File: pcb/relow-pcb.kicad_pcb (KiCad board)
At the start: 2 copper layers, 76.2 x 44.5 mm, 75 parts, among them IC1 AD8495, IC2 ATMEGA328P_TQFP, IC3 FT230X_SOP, J1 MICROUSB, J2 TOASTER, K1 S212S01, M3 VAL**, P1 AVR_ISP, Q1 MMBT4401, Q2 MMBT4401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

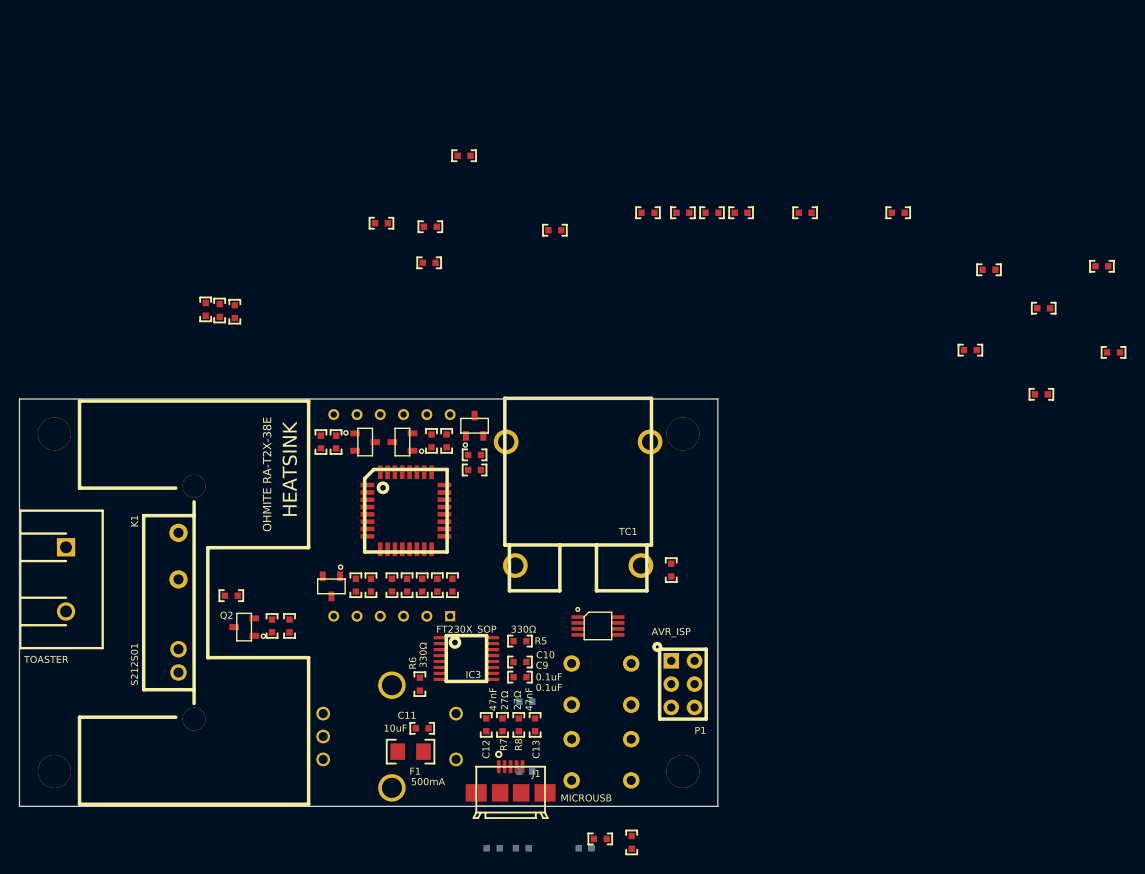
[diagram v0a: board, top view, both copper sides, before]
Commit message: components placed. starting traces
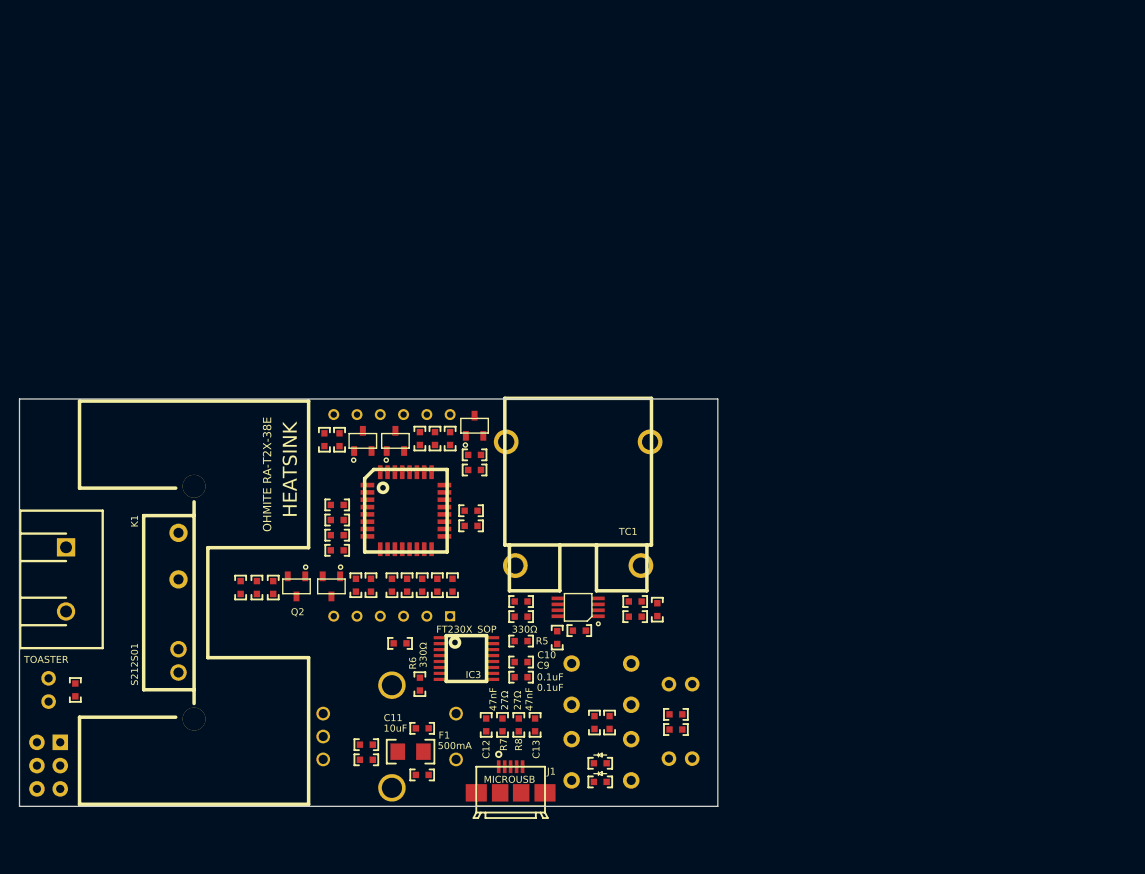
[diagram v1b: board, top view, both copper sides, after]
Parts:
- removed M3 (x4): VAL**, M3
- LED1, LED2: moved to F.Cu
- LED3, LED4, LED5: footprint 0603(1608m)_led -> LED-5mm
- P1: moved to B.Cu
- R18: value 1kΩ -> 330Ω
- moved R11 85.4 mm to (137.5, 157.1)
- moved R1 84.1 mm to (141.2, 146.1)
- moved R10 79.6 mm to (137.5, 158.8)
- moved R9 79.3 mm to (143.6, 160.4), turned to 180 degrees
- moved R14 74.5 mm to (162.4, 154.7), turned to 90 degrees
- moved R18 72.1 mm to (105.8, 151.1), turned to 90 degrees
- moved P1 69.8 mm to (102.9, 159.4), turned to 180 degrees
- moved R12 65.5 mm to (164.1, 154.7), turned to 90 degrees
- moved LED5 61.0 mm to (102.9, 151.1), turned to 270 degrees
- moved C3 55.4 mm to (134.4, 132.6)
- moved C1 53.7 mm to (158.4, 145.4), turned to 90 degrees
- moved C6 51.9 mm to (134.4, 130.9)
- moved R3 51.2 mm to (166.9, 141.5), turned to 180 degrees
- moved C5 48.1 mm to (166.9, 143.1), turned to 180 degrees
- moved R2 44.0 mm to (154.4, 141.5)
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
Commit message: laying traces like it's my job
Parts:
- turned C13 to 270 degrees
- turned R15 to 180 degrees
- turned R30 to 180 degrees
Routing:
- net GND: track 0.00 -> 39.4 mm
- net VCC: track 0.00 -> 38.5 mm
- net /HEAT: track 0.00 -> 18.1 mm
- net /DIG3: track 0.00 -> 14.4 mm
- net N-0000053: track 0.00 -> 8.99 mm
- net N-0000018: track 0.00 -> 7.82 mm
- net N-0000030: track 0.00 -> 7.79 mm
- net /SCK: track 0.00 -> 7.73 mm
- net N-0000052: track 0.00 -> 7.63 mm
- net /DIG1: track 0.00 -> 7.37 mm
- net N-0000039: track 0.00 -> 7.35 mm
- net N-0000016: track 0.00 -> 7.05 mm
- net /START: track 0.00 -> 6.59 mm
- net /ENC_B: track 0.00 -> 6.27 mm
- net /DIG2: track 0.00 -> 6.25 mm
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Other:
- net class Default: via_dia 0.889 -> 0.762; via_drill 0.635 -> 0.381
- rule trace_min: 0.254 -> 0.1524
- rule via_min_drill: 0.508 -> 0.3302
- rule via_min_size: 0.889 -> 0.6858

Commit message: layout done. ready to order (after triple checking)
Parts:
- added M3: VAL**, M3, B.Cu at (172.1, 160.0)
- added M3: VAL**, M3, B.Cu at (172.1, 123.2)
- added M3: VAL**, M3, B.Cu at (103.5, 160.0)
- added M3: VAL**, M3, B.Cu at (103.5, 123.2)
- IC2: value ATMEGA328P_TQFP -> ATMEGA328P
- IC3: value FT230X_SOP -> FT230X
- J1: value MICROUSB -> USB
- J2: footprint 2-PIN_SCREW-TERM_P7.5MM -> 2-PIN_SCREW-TERM_P200MIL
- P1: moved to F.Cu
- R1, R10, R11, R12, R14, R9: value 10kΩ_opt -> opt10kΩ
- moved P1 75.6 mm to (173.1, 131.4), turned to 0 degrees
- moved LED5 5.71 mm to (108.3, 149.5)
- moved R18 5.21 mm to (110.9, 150.0)
- moved LED3 4.58 mm to (172.1, 154.1)
- moved R13 3.39 mm to (172.1, 152.1), turned to 0 degrees
- moved R15 3.39 mm to (172.1, 150.5), turned to 0 degrees
- moved J2 3.03 mm to (103.1, 136.5)
- moved C1 2.33 mm to (160.5, 144.5), turned to 180 degrees
- moved LED4 1.92 mm to (172.1, 148.6)
- moved C4 1.55 mm to (160.5, 146.2)
- moved R14 1.53 mm to (162.3, 153.2)
- moved R12 1.52 mm to (164.1, 153.2)
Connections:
- LED3 pad 1: GND -> N-000002
- LED3 pad 2: N-000002 -> /LED_START
- LED4 pad 1: GND -> N-000003
- LED4 pad 2: N-000003 -> /LED_STOP
- R13 pad 1: N-000002 -> GND
- R13 pad 2: /LED_START -> N-000002
- R15 pad 1: N-000003 -> GND
- R15 pad 2: /LED_STOP -> N-000003
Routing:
- net GND: track 39.4 -> 403.1 mm, vias 0 -> 34
- net VCC: track 38.5 -> 242.9 mm, vias 0 -> 3
- net /STOP: track 6.09 -> 117.7 mm, vias 0 -> 1
- net /START: track 6.59 -> 90.0 mm, vias 0 -> 1
- net /RESET: track 0.00 -> 76.7 mm, vias 0 -> 2
- net /SET: track 3.70 -> 57.9 mm, vias 0 -> 1
- net /LED_STOP: track 0.00 -> 52.3 mm, vias 0 -> 1
- net /LED_START: track 0.00 -> 49.4 mm, vias 0 -> 1
- net /ENC_A: track 4.02 -> 48.6 mm, vias 0 -> 1
- net /ENC_B: track 6.27 -> 43.5 mm, vias 0 -> 1
- net /USART_RX: track 0.00 -> 35.3 mm, vias 0 -> 2
- net /MOSI: track 3.32 -> 37.9 mm, vias 0 -> 1
- net /MISO: track 3.49 -> 34.8 mm, vias 0 -> 1
- net /USART_TX: track 0.00 -> 28.9 mm, vias 0 -> 2
- net /SCK: track 7.73 -> 36.1 mm, vias 0 -> 1
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- added copper zone on B.Cu, net GND
- added copper zone on F.Cu, net GND
- added copper zone on B.Cu, net N-0000049
- added copper zone on F.Cu, net N-0000049
- added copper zone on B.Cu, net N-0000051
- added copper zone on F.Cu, net N-0000051
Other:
- outline, holes or cut-outs redrawn
- board text added: "<-AC!!!"
- board text added: "AC!!!"
- board text added: "CUT OUT"
- board text added: "github.com/mcous/reflow"
- board text added: "github.com/mcous/reflow open source hardware cc by-sa 3.0 mjc 11/5/13"
- board text added: "push to select"

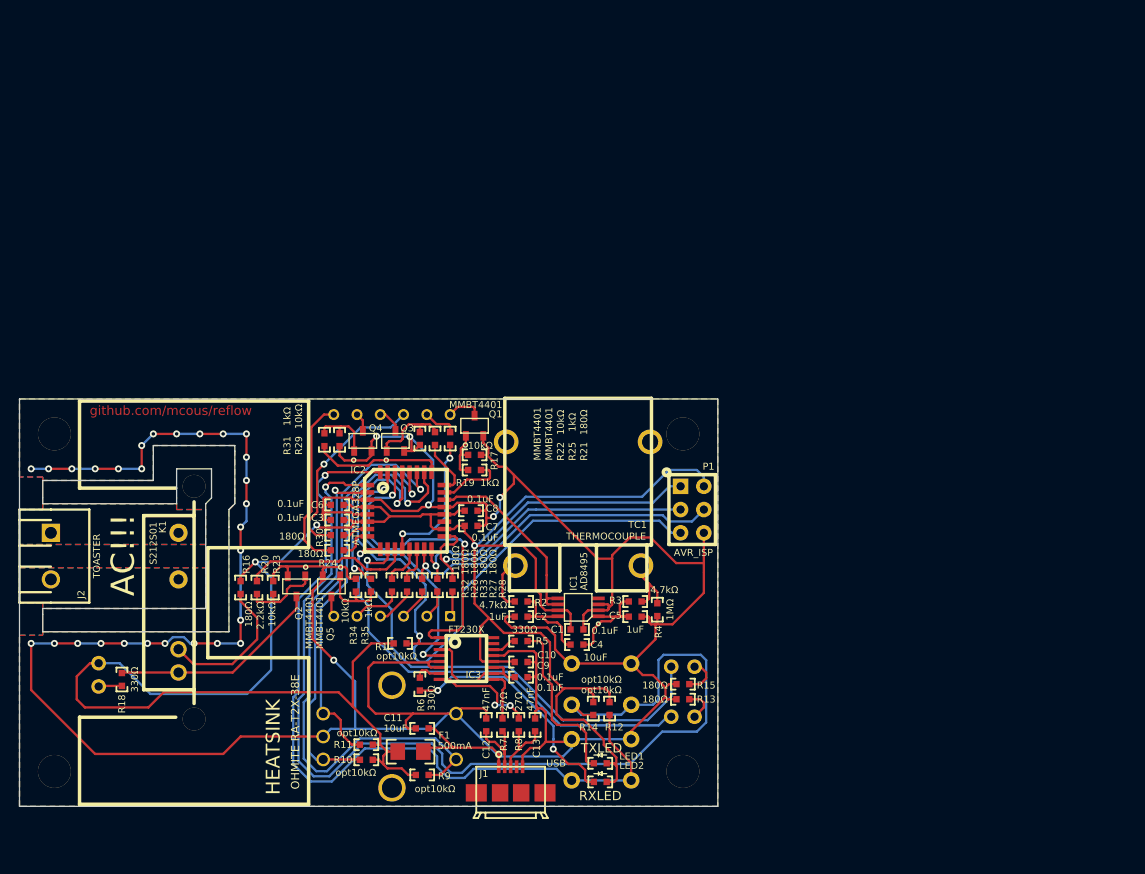
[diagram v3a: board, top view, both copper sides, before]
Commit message: minor trace changes and gerbers plotted
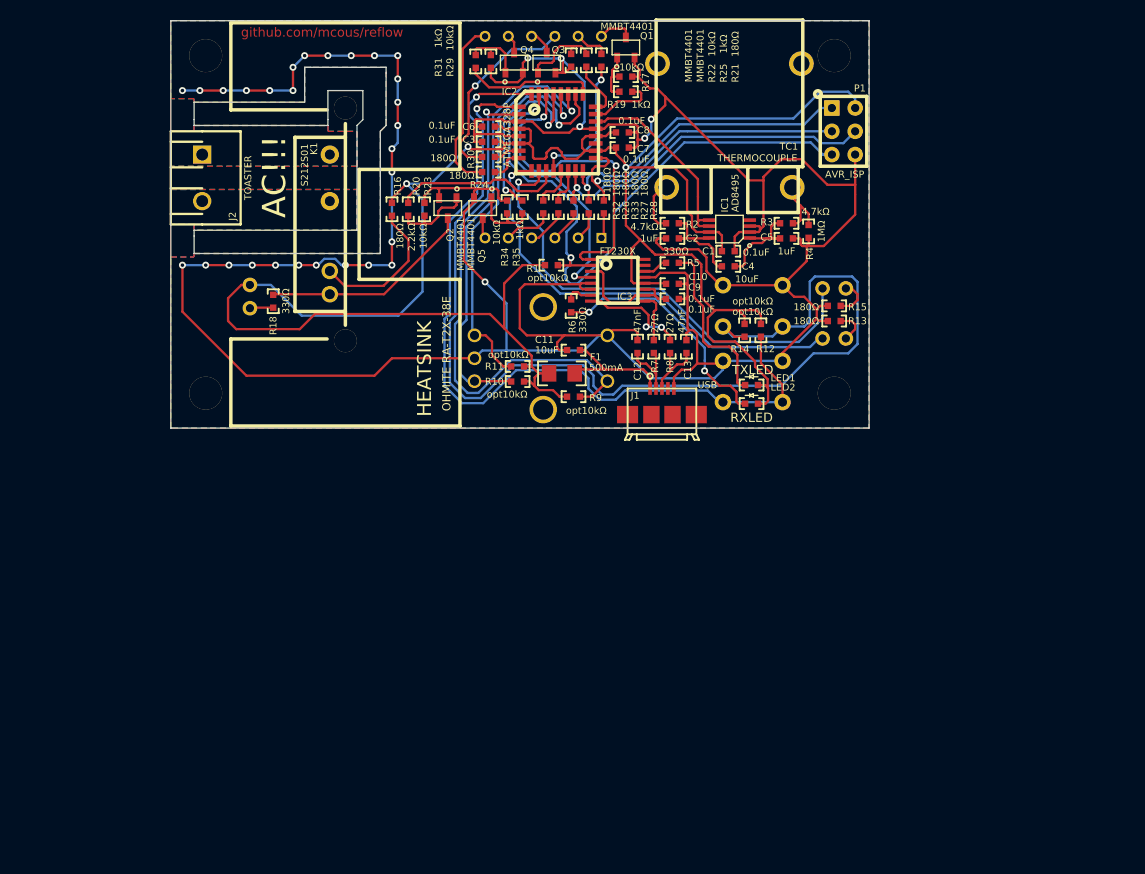
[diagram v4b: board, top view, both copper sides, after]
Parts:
- moved C7 44.5 mm to (165.5, 91.9)
- moved LED5 44.5 mm to (124.8, 108.2)
- moved C1 44.5 mm to (177.0, 103.3)
- moved C9 44.5 mm to (170.9, 108.5)
- moved J1 44.5 mm to (169.8, 121.0)
- moved J2 44.5 mm to (119.6, 95.2)
- moved M3 44.5 mm to (120.0, 118.7)
- moved R1 44.5 mm to (157.7, 104.8)
- moved R16 44.5 mm to (140.3, 98.7)
- moved R2 44.5 mm to (170.9, 100.2)
- moved R20 44.5 mm to (142.1, 98.7)
- moved R3 44.5 mm to (183.4, 100.2)
- moved R31 44.5 mm to (149.5, 82.5)
- moved S1 44.5 mm to (179.7, 117.5)
- moved S2 44.5 mm to (179.7, 109.2)
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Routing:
- net VCC: track 242.9 -> 245.8 mm
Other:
- rule pad_to_mask_clearance: 0 -> 0.0762

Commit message: going to bed again
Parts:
- moved M3 0.90 mm to (119.4, 81.3)
- moved M3 0.90 mm to (189.2, 81.3)
- moved M3 0.90 mm to (119.4, 119.4)
- moved M3 0.90 mm to (189.2, 119.4)
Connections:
- M3 pad 1: (no net) -> GND (x4)
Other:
- board text added: "(so, um, don't like, touch it)"
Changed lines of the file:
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@@
 (kicad_pcb (version 3) (host pcbnew "(2013-07-07 BZR 4022)-stable")
   (general
-    (links 154)
+    (links 158)
     (no_connects 0)
-    (area 88.758314 112.061001 185.106733 167.0304)
+    (area 105.268314 70.786001 201.616733 125.7554)
     (thickness 1.6)
-    (drawings 36)
+    (drawings 37)
     (tracks 1026)
     (zones 0)
@@
   (layers
     (15 F.Cu signal)
-    (0 B.Cu signal)
+    (0 B.Cu signal hide)
     (16 B.Adhes user)
     (17 F.Adhes user)
     (18 B.Paste user)
     (19 F.Paste user)
-    (20 B.SilkS user)
+    (20 B.SilkS user hide)
     (21 F.SilkS user)
     (22 B.Mask user)
@@
     (mod_text_size 0.762 0.762)
     (mod_text_width 0.1524)
-    (pad_size 2.1 1.3)
-    (pad_drill 0)
+    (pad_size 3.6 3.6)
+    (pad_drill 3.6)
     (pad_to_mask_clearance 0.0762)
     (aux_axis_origin 116.205 122.555)
-    (visible_elements 7FFFFFFF)
+    (visible_elements 7FFFBFFF)
     (pcbplotparams
-      (layerselection 3178497)
+      (layerselection 284196865)
       (usegerberextensions true)
       (excludeedgelayer true)
-      (linewidth 0.150000)
+      (linewidth 0.152400)
       (plotframeref false)
       (viasonmask false)
       (mode 1)
-      (useauxorigin false)
+      (useauxorigin true)
       (hpglpennumber 1)
       (hpglpenspeed 20)
@@
       (plotinvisibletext false)
       (padsonsilk false)
-      (subtractmaskfromsilk false)
+      (subtractmaskfromsilk true)
       (outputformat 1)
       (mirror false)
-      (drillshape 1)
+      (drillshape 0)
       (scaleselection 1)
-      (outputdirectory ""))
+      (outputdirectory plotted/))
   )
   (net 0 "")
@@
       (effects (font (size 0.762 0.762) (thickness 0.1524)) (justify mirror))
     )
-    (fp_text value START (at -9.525 3.175) (layer B.SilkS)
-      (effects (font (size 2.032 2.032) (thickness 0.4064)) (justify mirror))
+    (fp_text value START (at -8.89 1.27) (layer B.SilkS)
+      (effects (font (size 1.778 1.778) (thickness 0.3556)) (justify mirror))
     )
     (fp_line (start 3 -3) (end 4.5 -3) (layer B.SilkS) (width 0.381))
@@
       (effects (font (size 0.762 0.762) (thickness 0.1524)) (justify mirror))
     )
-    (fp_text value STOP (at -8.89 -1.905) (layer B.SilkS)
-      (effects (font (size 2.032 2.032) (thickness 0.4064)) (justify mirror))
+    (fp_text value STOP (at -8.255 -0.635) (layer B.SilkS)
+      (effects (font (size 1.778 1.778) (thickness 0.3556)) (justify mirror))
     )
     (fp_line (start 3 -3) (end 4.5 -3) (layer B.SilkS) (width 0.381))
@@
   (module MSOP8 (layer F.Cu)
     (at 177.165 100.838 180)
-    (solder_mask_margin 0.1)
-    (solder_paste_margin -0.025)
-    (clearance 0.15)
+    (clearance 0.2286)
     (attr smd)
     (fp_text reference IC1 (at 0.508 2.667 270) (layer F.SilkS)
@@
   (module MICROUSB_sm (layer F.Cu)
     (at 169.799 121.031 90)
-    (solder_mask_margin 0.1)
-    (solder_paste_margin -0.025)
-    (clearance 0.15)
+    (clearance 0.2286)
     (attr smd)
     (fp_text reference J1 (at 2.032 -2.921 180) (layer F.SilkS)
@@
     )
   )
-  (module M3   locked (layer B.Cu)
-    (at 188.595 118.745)
-    (fp_text reference M3 (at 2.667 3.048) (layer B.SilkS)
+  (module M3 (layer B.Cu)
+    (at 189.23 119.38)
+    (fp_text reference M3 (at -3.81 1.905) (layer B.SilkS)
       (effects (font (size 0.762 0.762) (thickness 0.1524)) (justify mirror))
     )
@@
     (pad 1 thru_hole circle (at 0 0) (size 3.6 3.6) (drill 3.6)
       (layers *.Cu *.SilkS *.Mask)
-    )
-  )
-  (module M3   locked (layer B.Cu)
-    (at 188.595 81.915)
-    (fp_text reference M3 (at 2.667 -2.921) (layer B.SilkS)
+      (net 25 GND)
+    )
+  )
+  (module M3 (layer B.Cu)
+    (at 189.23 81.28)
+    (fp_text reference M3 (at -3.175 -2.54) (layer B.SilkS)
       (effects (font (size 0.762 0.762) (thickness 0.1524)) (justify mirror))
     )
@@
     (pad 1 thru_hole circle (at 0 0) (size 3.6 3.6) (drill 3.6)
       (layers *.Cu *.SilkS *.Mask)
-    )
-  )
-  (module M3   locked (layer B.Cu)
-    (at 120.015 118.745)
-    (fp_text reference M3 (at -2.667 3.048) (layer B.SilkS)
+      (net 25 GND)
+    )
+  )
+  (module M3 (layer B.Cu)
+    (at 119.38 119.38)
+    (fp_text reference M3 (at 1.905 -3.175) (layer B.SilkS)
       (effects (font (size 0.762 0.762) (thickness 0.1524)) (justify mirror))
     )
@@
     (pad 1 thru_hole circle (at 0 0) (size 3.6 3.6) (drill 3.6)
       (layers *.Cu *.SilkS *.Mask)
-    )
-  )
-  (module M3   locked (layer B.Cu)
-    (at 120.015 81.915)
-    (fp_text reference M3 (at -2.667 -2.921) (layer B.SilkS)
+      (net 25 GND)
+    )
+  )
+  (module M3 (layer B.Cu)
+    (at 119.38 81.28)
+    (fp_text reference M3 (at -1.905 3.175) (layer B.SilkS)
       (effects (font (size 0.762 0.762) (thickness 0.1524)) (justify mirror))
     )
@@
     (pad 1 thru_hole circle (at 0 0) (size 3.6 3.6) (drill 3.6)
       (layers *.Cu *.SilkS *.Mask)
-    )
+      (net 25 GND)
+    )
+  )
+  (gr_text "(so, um, don't\nlike, touch it)" (at 120.015 106.045 90) (layer B.SilkS)
+    (effects (font (size 0.762 0.762) (thickness 0.1524)) (justify left mirror))
   )
   (gr_text "github.com/mcous/reflow\nopen source hardware\ncc by-sa 3.0\nmjc 11/5/13\n" (at 123.825 116.205) (layer B.SilkS)

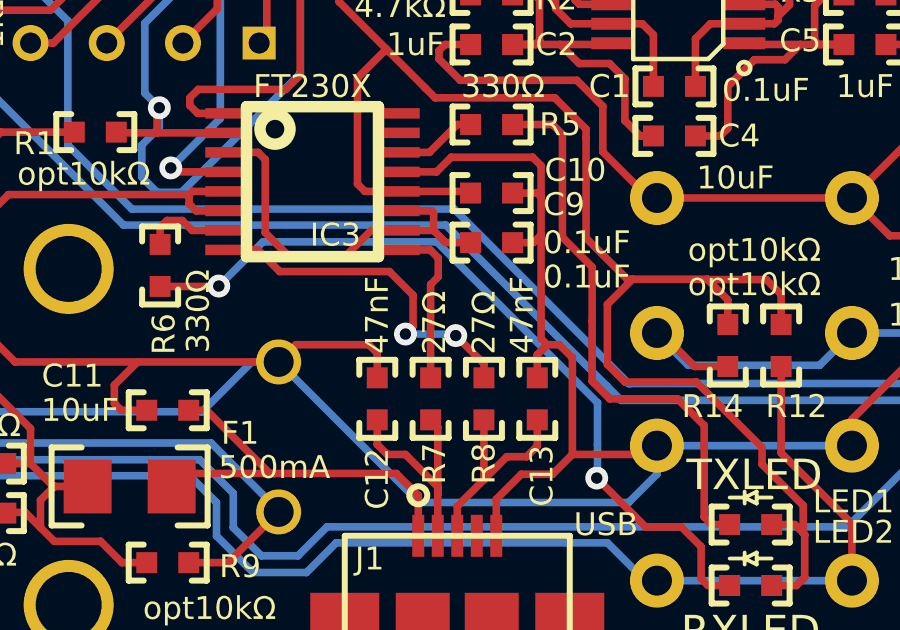
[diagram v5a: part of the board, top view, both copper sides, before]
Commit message: USB caps should be 47pF, not 47nF
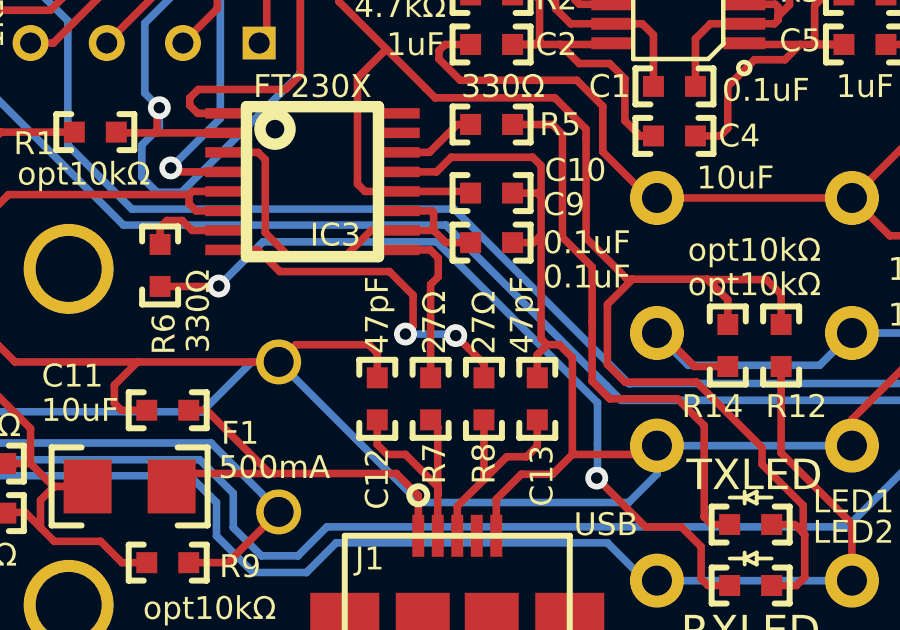
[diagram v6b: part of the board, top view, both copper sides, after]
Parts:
- C12, C13: value 47nF -> 47pF
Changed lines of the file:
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@@
     (links 158)
     (no_connects 0)
-    (area 105.268314 70.786001 201.616733 125.7554)
+    (area 105.268314 70.786001 202.251733 126.3904)
     (thickness 1.6)
     (drawings 37)
@@
       (effects (font (size 0.762 0.762) (thickness 0.1524)))
     )
-    (fp_text value 47nF (at -2.794 0 270) (layer F.SilkS)
+    (fp_text value 47pF (at -2.794 0 270) (layer F.SilkS)
       (effects (font (size 0.762 0.762) (thickness 0.1524)))
     )
@@
       (effects (font (size 0.762 0.762) (thickness 0.1524)))
     )
-    (fp_text value 47nF (at -2.794 0.508 270) (layer F.SilkS)
-      (effects (font (size 0.762 0.762) (thickness 0.1524)))
-    )
+    (fp_text value 47pF (at -2.794 0.508 270) (layer F.SilkS)
+      (effects (font (size 0.762 0.762) (thickness 0.1524)))
+    )
